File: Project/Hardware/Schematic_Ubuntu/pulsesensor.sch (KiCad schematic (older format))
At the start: 2 parts, among them U4 Pulse_sensor

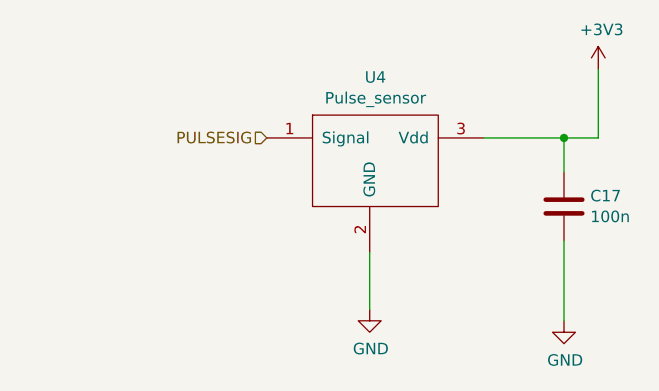
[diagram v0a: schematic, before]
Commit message: Extra resistor till temp gain, två cubemx project med olika pinsmaps, Gerber filer till pcb_revS
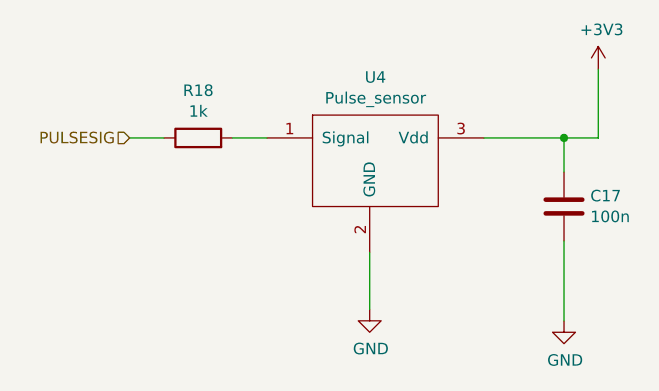
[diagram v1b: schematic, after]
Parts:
- added R18: 1k, Resistors_SMD:R_0805_HandSoldering, symbol Device:R
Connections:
- net PULSESIG: now also R18.1; no longer U4.1 (Signal)
- new net: R18.2, U4.1 (Signal)
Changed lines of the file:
@@
 Wire Wire Line
 	2400 2300 2400 2550
-Text HLabel 1950 1800 0    50   Input ~ 0
+Text HLabel 1350 1800 0    50   Input ~ 0
 PULSESIG
+$Comp
+L Device:R R18
+U 1 1 5C66D3BB
+P 1650 1800
+F 0 "R18" V 1857 1800 50  0000 C CNN
+F 1 "1k" V 1766 1800 50  0000 C CNN
+F 2 "Resistors_SMD:R_0805_HandSoldering" V 1580 1800 50  0001 C CNN
+F 3 "~" H 1650 1800 50  0001 C CNN
+	1    1650 1800
+	0    -1   -1   0
+$EndComp
+Wire Wire Line
+	1800 1800 1950 1800
+Wire Wire Line
+	1500 1800 1350 1800
 $EndSCHEMATC
